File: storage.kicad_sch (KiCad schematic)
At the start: 15 parts, among them J1 Micro_SD_Card_Det1, U1 MX6UL-VM, U8 D5V0H1B2LP, U9 W25Q32JVZP

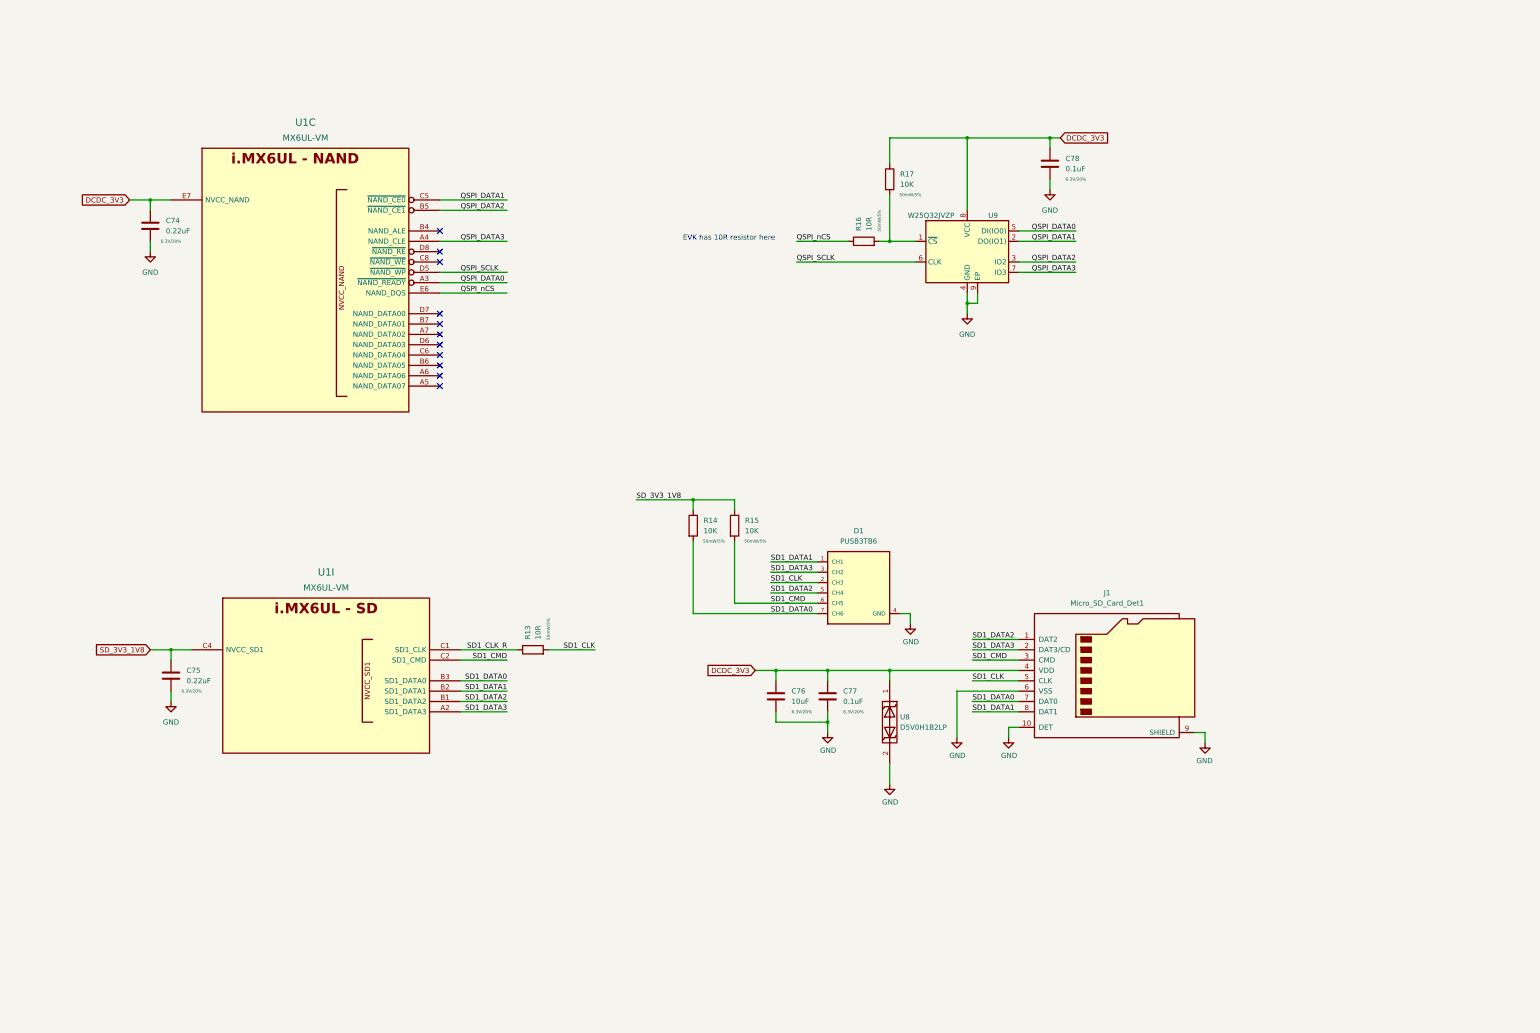
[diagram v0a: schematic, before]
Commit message: more ddr routing, add more connectors
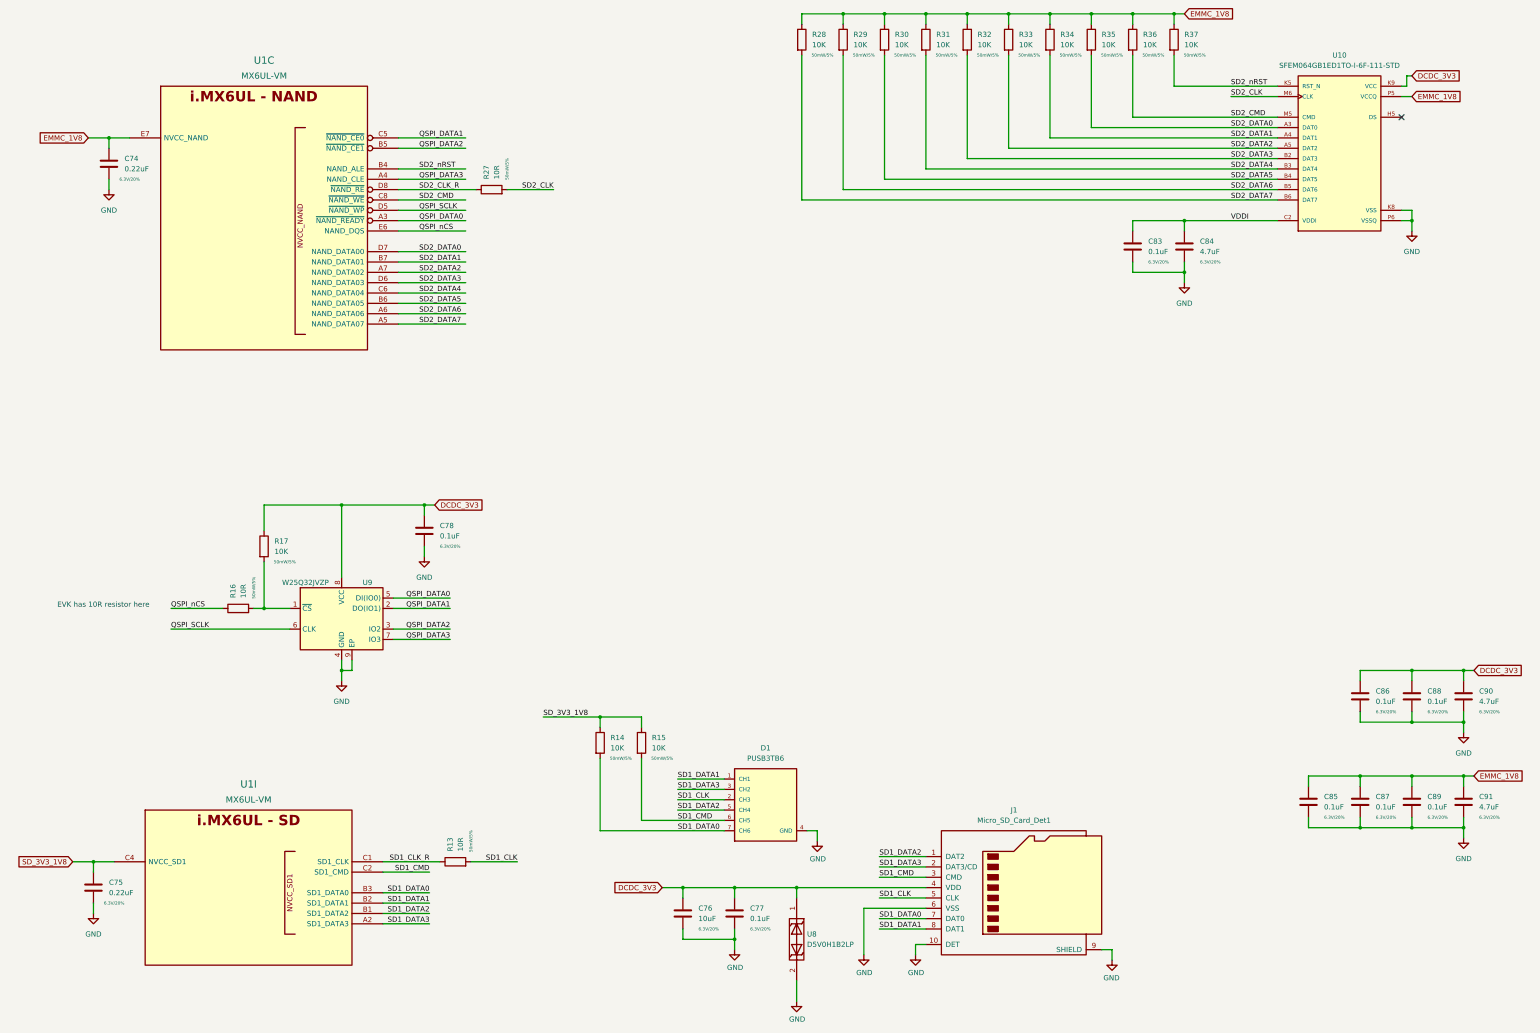
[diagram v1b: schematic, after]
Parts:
- added C83, C85, C86, C87, C88, C89: 0.1uF, Capacitor_SMD:C_0402_1005Metric, symbol Device:C
- added C84, C90, C91: 4.7uF, Capacitor_SMD:C_0402_1005Metric, symbol Device:C
- added R27: 10R, Resistor_SMD:R_0402_1005Metric, symbol Device:R
- added R28, R29, R30, R31, R32, R33, R34, R35, R36, R37: 10K, Resistor_SMD:R_0402_1005Metric, symbol Device:R
- added U10: SFEM064GB1ED1TO-I-6F-111-STD, imx6ull-sbc:BGA153N50P14X14_1150X1300X100, symbol imx6ull-sbc:SFEM064GB1ED1TO-I-6F-111-STD
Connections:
- net GND: now also C83.2, C84.2, C85.2, C86.2, C87.2, C88.2, C89.2, C90.2, C91.2, U10.A6 (VSS), U10.C4 (VSSQ), U10.E7 (VSS), U10.G5 (VSS), U10.H10 (VSS), U10.J5 (VSS), U10.K8 (VSS), U10.N2 (VSSQ), U10.N5 (VSSQ), U10.P4 (VSSQ), U10.P6 (VSSQ)
- net SD2_DATA7: now reaches U1.A5 (NAND_DATA07)
- net SD2_DATA7: now also R28.2, U10.B6 (DAT7)
- net SD2_DATA6: now reaches U1.A6 (NAND_DATA06)
- net SD2_DATA6: now also R29.2, U10.B5 (DAT6)
- net SD2_DATA2: now reaches U1.A7 (NAND_DATA02)
- net SD2_DATA2: now also R33.2, U10.A5 (DAT2)
- net SD2_nRST: now reaches U1.B4 (NAND_ALE)
- net SD2_nRST: now also R37.2, U10.K5 (RST_N)
- net SD2_DATA5: now reaches U1.B6 (NAND_DATA05)
- net SD2_DATA5: now also R30.2, U10.B4 (DAT5)
- net SD2_DATA1: now reaches U1.B7 (NAND_DATA01)
- net SD2_DATA1: now also R34.2, U10.A4 (DAT1)
- net SD2_DATA4: now reaches U1.C6 (NAND_DATA04)
- net SD2_DATA4: now also R31.2, U10.B3 (DAT4)
- net SD2_CMD: now reaches U1.C8 (~{NAND_WE})
- net SD2_CMD: now also R36.2, U10.M5 (CMD)
- net SD2_DATA3: now reaches U1.D6 (NAND_DATA03)
- net SD2_DATA3: now also R32.2, U10.B2 (DAT3)
- net SD2_DATA0: now reaches U1.D7 (NAND_DATA00)
- net SD2_DATA0: now also R35.2, U10.A3 (DAT0)
- net SD2_CLK_R: now reaches U1.D8 (~{NAND_RE})
- net SD2_CLK_R: now also R27.1
- net DCDC_3V3 renamed VCC
- net VCC: now also C86.1, C88.1, C90.1, U10.E6 (VCC), U10.F5 (VCC), U10.J10 (VCC), U10.K9 (VCC); no longer C74.1, U1.E7 (NVCC_NAND)
- new net SD2_CLK: R27.2, U10.M6 (CLK)
- new net VCCQ: C74.1, C85.1, C87.1, C89.1, C91.1, R28.1, R29.1, R30.1, R31.1, R32.1, R33.1, R34.1, R35.1, R36.1, R37.1, U1.E7 (NVCC_NAND), U10.C6 (VCCQ), U10.M4 (VCCQ), U10.N4 (VCCQ), U10.P3 (VCCQ), U10.P5 (VCCQ)
- new net VDDI: C83.1, C84.1, U10.C2 (VDDI)
- no-connect marks 11 -> 1
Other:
- moved on the sheet: C74, C75, C76, C77, C78, D1, J1, R13, R14, R15, R16, R17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

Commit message: start moving to hierarchal labels, add emmc
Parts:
- removed R16: 10R, Resistor_SMD:R_0402_1005Metric, symbol Device:R
- added U?: SFEM064GB1ED1TO-I-6F-111-STD, symbol imx6ull-sbc:SFEM064GB1ED1TO-I-6F-111-STD
- U10: footprint imx6ull-sbc:BGA153N50P14X14_1150X1300X100 -> imx6ull-sbc:FBGA-153; MANUFACTURER Swissbit -> (none)
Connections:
- net QSPI_nCS: now also R17.2, U9.1 (~{CS})
- net SD2_CMD: now also R37.2; no longer R36.2
- net SD2_nRST: now also R36.2; no longer R37.2
- net VCC renamed DCDC_3V3
- net VCCQ renamed EMMC_1V8
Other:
- note removed: "EVK has 10R resistor here"
- moved on the sheet: C74, C78, C83, C84, C85, C86, C87, C88, C89, C90, C91, R17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

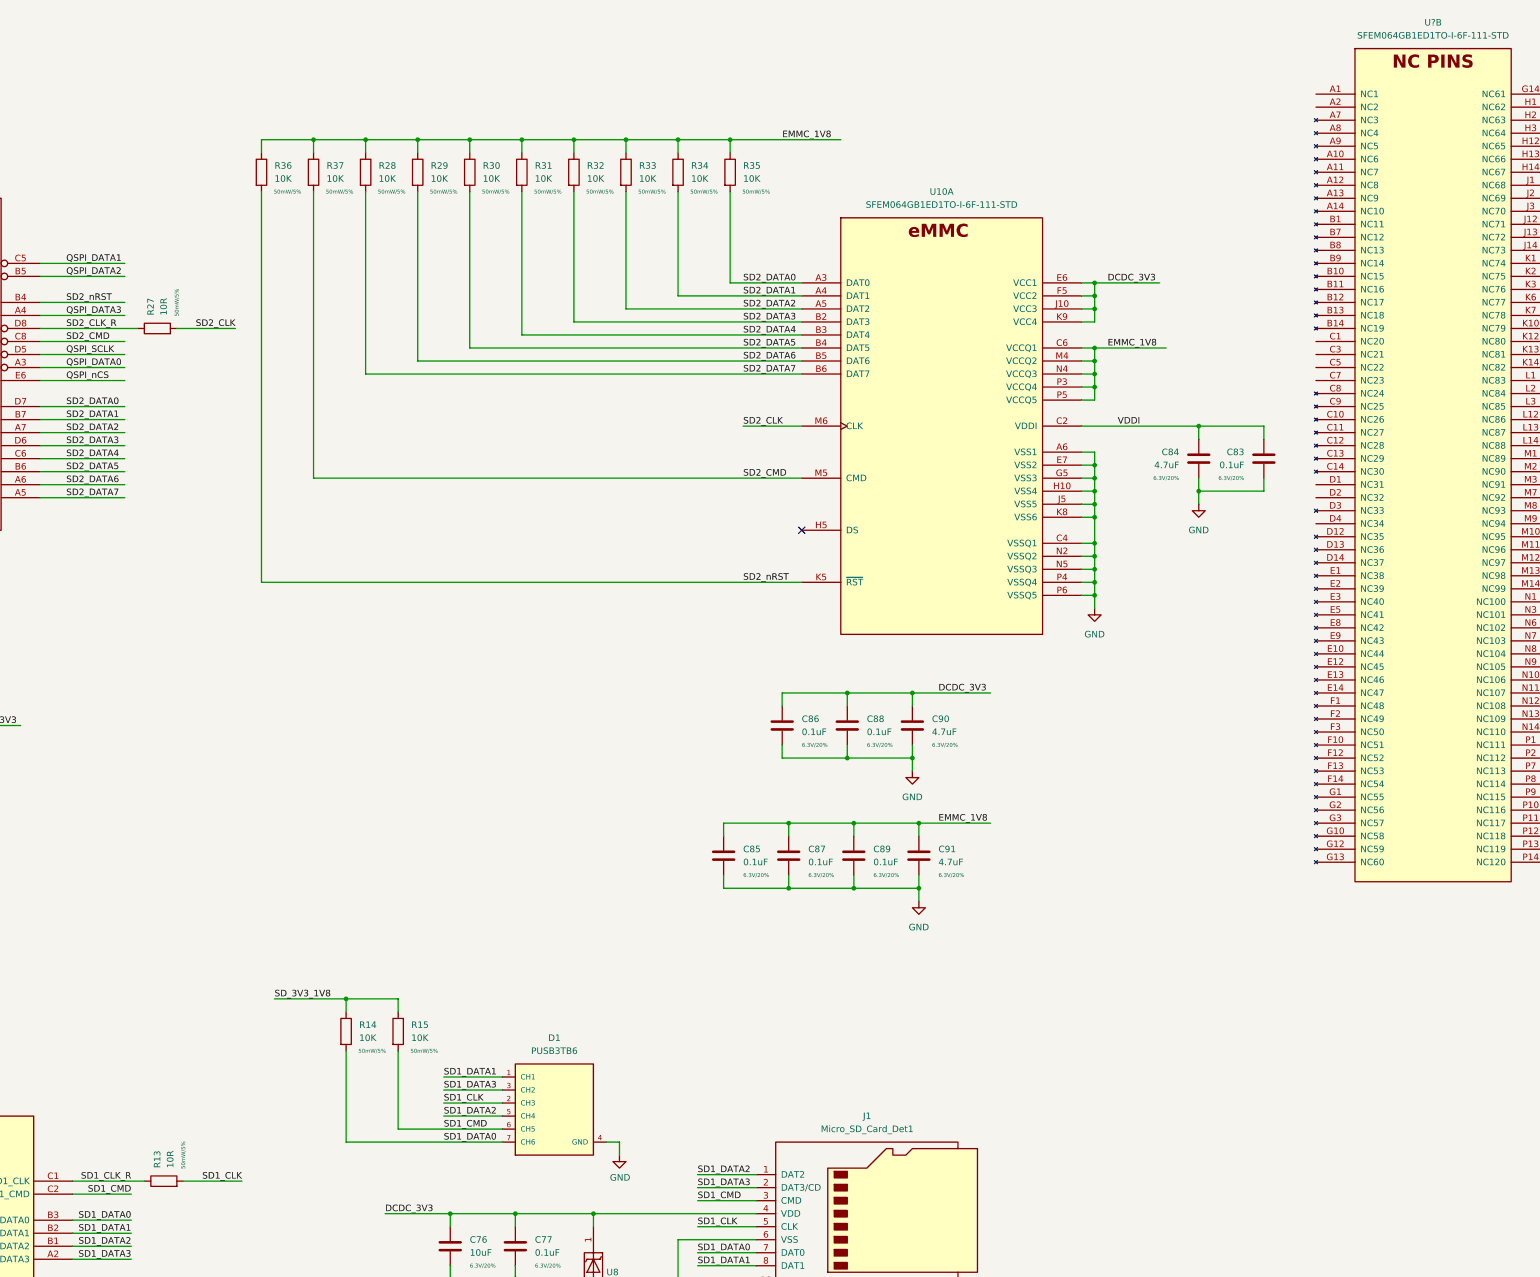
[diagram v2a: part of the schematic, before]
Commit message: move to hierarchal labels, work on power tree, add basic pcb layout
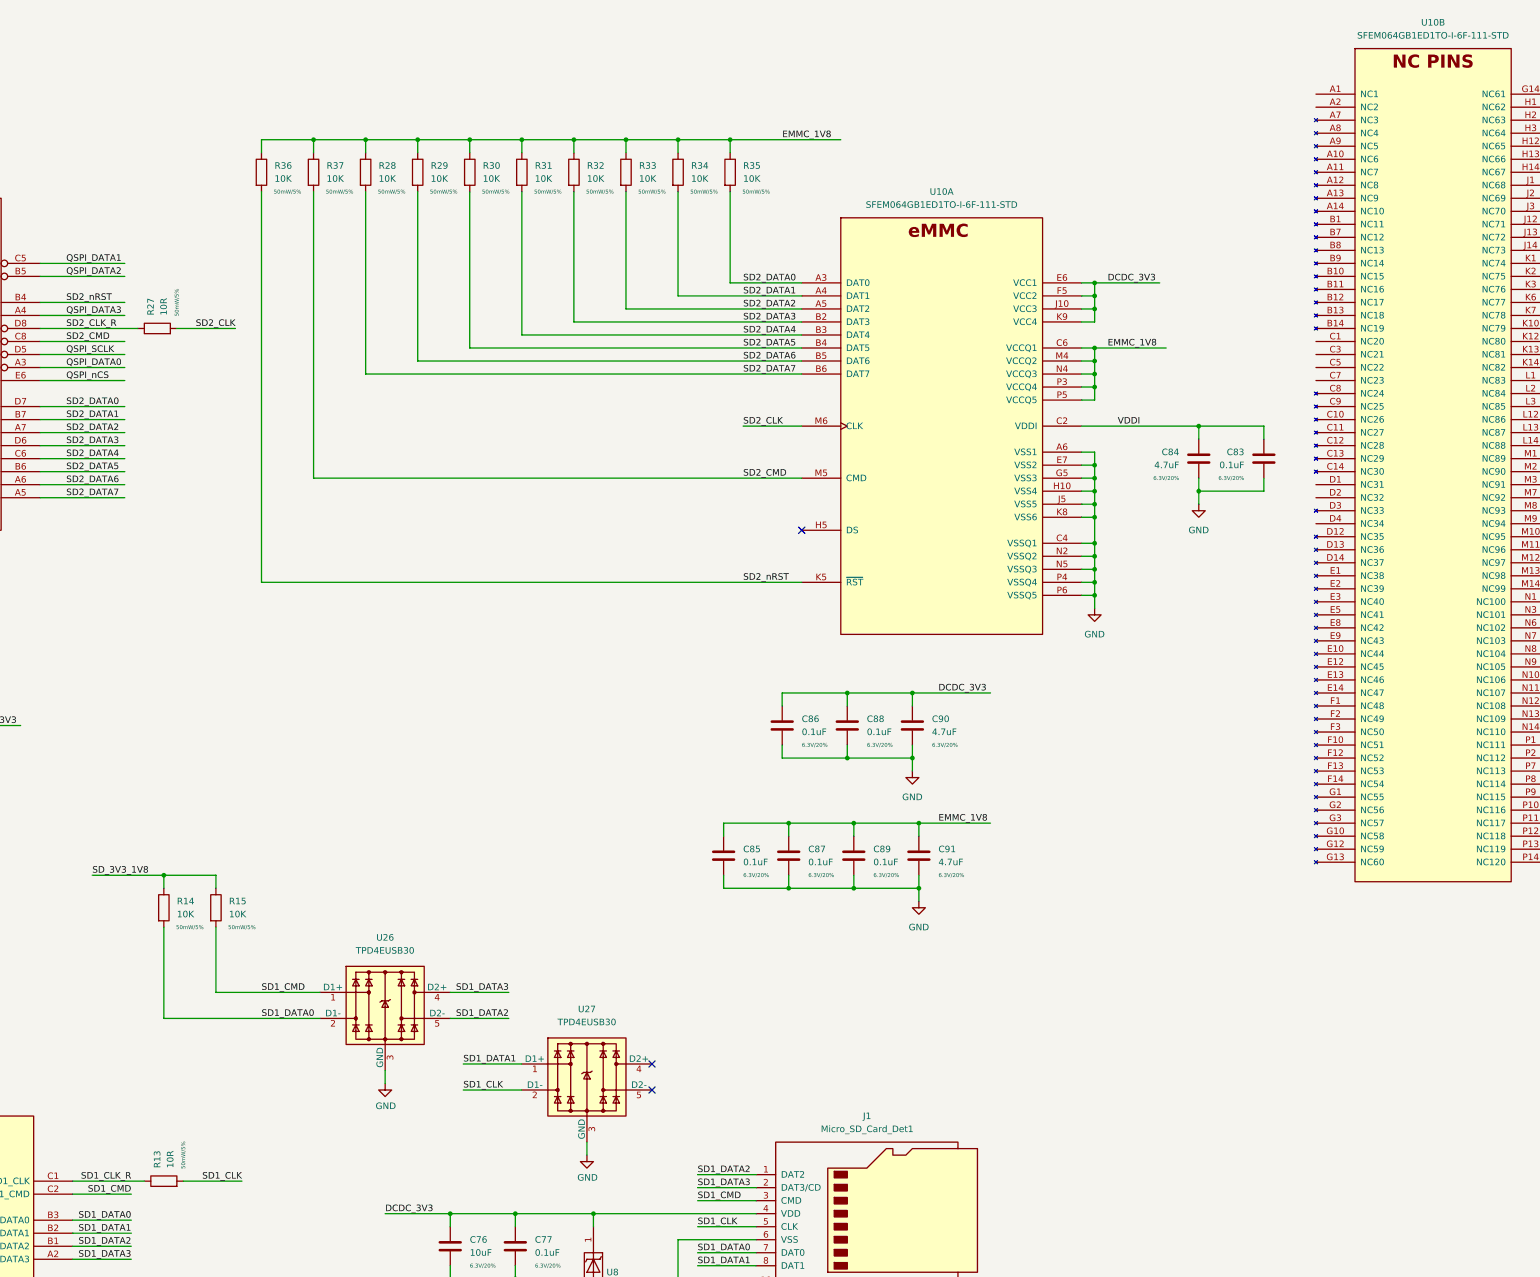
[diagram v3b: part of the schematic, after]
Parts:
- removed D1: PUSB3TB6, imx6ull-sbc:SOT1358-1, symbol imx6ull-sbc:PUSB3TB6
- added U26, U27: TPD4EUSB30, Package_SON:USON-10_2.5x1.0mm_P0.5mm, symbol imx6ull-sbc:TPD4EUSB30
- U10: renamed from U?; footprint (none) -> imx6ull-sbc:FBGA-153
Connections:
- net GND: now also U26.3 (GND), U26.8 (GND), U27.3 (GND), U27.8 (GND)
- net SD1_CLK: now also U27.2 (D1-), U27.9
- net SD1_CMD: now also U26.1 (D1+), U26.10
- net SD1_DATA0: now also U26.2 (D1-), U26.9
- net SD1_DATA1: now also U27.1 (D1+), U27.10
- net SD1_DATA2: now also U26.5 (D2-), U26.6
- net SD1_DATA3: now also U26.4 (D2+), U26.7
- new net: U27.4 (D2+), U27.7
- new net: U27.5 (D2-), U27.6
- no-connect marks 1 -> 3
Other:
- moved on the sheet: R14, R15

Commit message: lots of routing, ddr length matching done
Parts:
- removed C83, C85, C86, C87, C88, C89: 0.1uF, Capacitor_SMD:C_0402_1005Metric, symbol Device:C
- removed C84, C90, C91: 4.7uF, Capacitor_SMD:C_0402_1005Metric, symbol Device:C
- removed R27: 10R, Resistor_SMD:R_0402_1005Metric, symbol Device:R
- removed R28, R29, R30, R31, R32, R33, R34, R35, R36, R37: 10K, Resistor_SMD:R_0402_1005Metric, symbol Device:R
- removed U10: SFEM064GB1ED1TO-I-6F-111-STD, imx6ull-sbc:FBGA-153, symbol imx6ull-sbc:SFEM064GB1ED1TO-I-6F-111-STD
- C74, C75: footprint Capacitor_SMD:C_0402_1005Metric -> Capacitor_SMD:C_0201_0603Metric
- J1: footprint imx6ull-sbc:GCT_MEM2051-00-195-00-A_REVC -> qsbc-zero:GCT_MEM2051-00-195-00-A_REVC; symbol imx6ull-sbc:Micro_SD_Card_Det1 -> qsbc-zero:Micro_SD_Card_Det1
- U1: footprint imx6ull-sbc:SOT1534-2 -> qsbc-zero:SOT1534-2; symbol imx6ull-sbc:MX6UL-VM -> qsbc-zero:MX6UL-VM
- U26, U27: symbol imx6ull-sbc:TPD4EUSB30 -> qsbc-zero:TPD4EUSB30
- U8: footprint imx6ull-sbc:DFN100X60X45-2N -> qsbc-zero:DFN100X60X45-2N; symbol imx6ull-sbc:D5V0H1B2LP -> qsbc-zero:D5V0H1B2LP
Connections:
- net DCDC_3V3: now also C74.1, U1.E7 (NVCC_NAND)
- net EMMC_1V8: no longer C74.1, U1.E7 (NVCC_NAND)
- net SD1_CMD: now also U27.1 (D1+), U27.10; no longer U26.1 (D1+), U26.10
- net SD1_DATA1: now also U26.1 (D1+), U26.10; no longer U27.1 (D1+), U27.10
- net SD2_CLK_R: no longer names the net of U1.D8 (~{NAND_RE})
- net SD2_CMD: no longer names the net of U1.C8 (~{NAND_WE})
- net SD2_DATA0: no longer names the net of U1.D7 (NAND_DATA00)
- net SD2_DATA1: no longer names the net of U1.B7 (NAND_DATA01)
- net SD2_DATA2: no longer names the net of U1.A7 (NAND_DATA02)
- net SD2_DATA3: no longer names the net of U1.D6 (NAND_DATA03)
- net SD2_DATA4: no longer names the net of U1.C6 (NAND_DATA04)
- net SD2_DATA5: no longer names the net of U1.B6 (NAND_DATA05)
- net SD2_DATA6: no longer names the net of U1.A6 (NAND_DATA06)
- net SD2_DATA7: no longer names the net of U1.A5 (NAND_DATA07)
- net SD2_nRST: no longer names the net of U1.B4 (NAND_ALE)
- no-connect marks 3 -> 13
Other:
- moved on the sheet: U27

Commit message: more pcb work, bom work
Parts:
- C74, C75: DigiKey_PN (none) -> 490-10392-1-ND; MPN (none) -> GRM033C80J224KE90D
- C76: DigiKey_PN (none) -> 490-GRM155R60J106ME05DCT-ND; MPN (none) -> GRM155R60J106ME05D
- C77, C78: DigiKey_PN (none) -> 490-14603-1-ND; MPN (none) -> GRM155R71E104KE14J; Rating 6.3V/20% -> 25V/20%
- J1: MPN (none) -> MEM2051-00-195-00-A
- R13: DigiKey_PN (none) -> 311-10JRCT-ND; MPN (none) -> RC0402JR-0710RL
- R14, R15, R17: DigiKey_PN (none) -> 311-10KJRCT-ND; MPN (none) -> RC0402JR-0710KL
- U1: DigiKey_PN (none) -> 568-14995-ND; MPN (none) -> MCIMX6Y2DVM09AB
- U26, U27: DigiKey_PN (none) -> 296-28063-1-ND; MPN (none) -> TPD4EUSB30DQAR
- U8: DigiKey_PN (none) -> D5V0H1B2LP-7BDICT-ND; MPN (none) -> D5V0H1B2LP-7B
- U9: value W25Q32JVZP -> W25Q256JWPIQ; DigiKey_PN (none) -> 256-W25Q256JWPIQ-ND; MPN (none) -> W25Q256JWPIQ
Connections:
- net GND: no longer J1.10 (DET)
- net SD1_CD: now reaches U27.4 (D2+), U27.7
- net SD1_CD: now also J1.10 (DET)
- no-connect marks 13 -> 12

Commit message: add basic readme, rev 1 of pcb
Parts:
- added J11: Conn_01x09_Male, Connector_PinHeader_1.27mm:PinHeader_1x09_P1.27mm_Vertical, symbol Connector:Conn_01x09_Male
- U9: value W25Q256JWPIQ -> W25Q512JVEIQ; DigiKey_PN 256-W25Q256JWPIQ-ND -> W25Q512JVEIQ-ND; MPN W25Q256JWPIQ -> W25Q512JVEIQ
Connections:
- net DCDC_3V3: now also J11.1 (Pin_1)
- net GND: now also J11.9 (Pin_9)
- net ECSPI4_CS0: now reaches U1.A5 (NAND_DATA07)
- net ECSPI4_CS0: now also J11.7 (Pin_7)
- net ECSPI4_MISO: now reaches U1.A6 (NAND_DATA06)
- net ECSPI4_MISO: now also J11.6 (Pin_6)
- net ECSPI4_MOSI: now reaches U1.B6 (NAND_DATA05)
- net ECSPI4_MOSI: now also J11.5 (Pin_5)
- net ECSPI4_CS1: now reaches U1.B7 (NAND_DATA01)
- net ECSPI4_CS1: now also J11.8 (Pin_8)
- net ECSPI4_SCLK: now reaches U1.C6 (NAND_DATA04)
- net ECSPI4_SCLK: now also J11.4 (Pin_4)
- new net I2C2_SCL: J11.2 (Pin_2)
- new net I2C2_SDA: J11.3 (Pin_3)
- no-connect marks 12 -> 7

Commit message: misc fixes, add pics of board
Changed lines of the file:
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@@
   (no_connect (at 104.14 99.06))
   (no_connect (at 254 209.55))
+  (bus_entry (at 148.59 254) (size 2.54 2.54)
+    (stroke (width 0) (type default) (color 0 0 0 0))
+  )
+  (bus_entry (at 302.26 287.02) (size 2.54 2.54)
+    (stroke (width 0) (type default) (color 0 0 0 0))
+  )
   (wire (pts (xy 29.21 20.32) (xy 41.91 20.32))
     (stroke (width 0) (type default) (color 0 0 0 0))
@@
     (effects (font (size 1.27 1.27)) (justify left bottom))
   )
-  (label "SD1_CMD" (at 219.71 204.47 180)
-    (effects (font (size 1.27 1.27)) (justify right bottom))
+  (label "SD1_CMD" (at 217.17 204.47 0)
+    (effects (font (size 1.27 1.27)) (justify left bottom))
   )
   (label "ECSPI4_CS0" (at 106.68 109.22 0)
